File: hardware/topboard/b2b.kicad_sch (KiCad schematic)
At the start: 14 parts

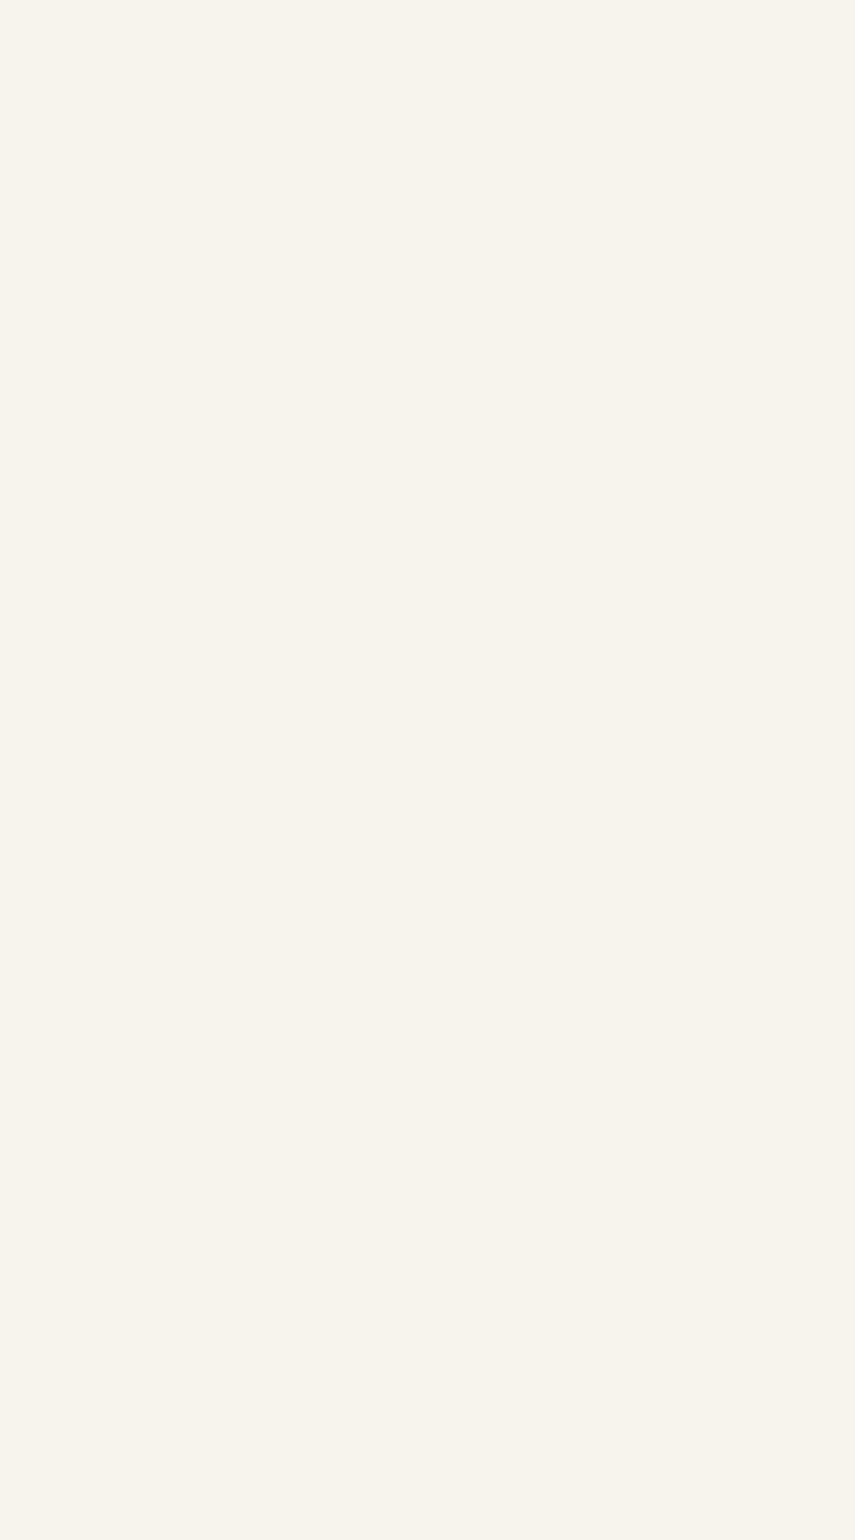
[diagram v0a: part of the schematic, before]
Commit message: Initial pin plan for front b2b connector
Signed-off-by: gatecat <gatecat@ds0.me>
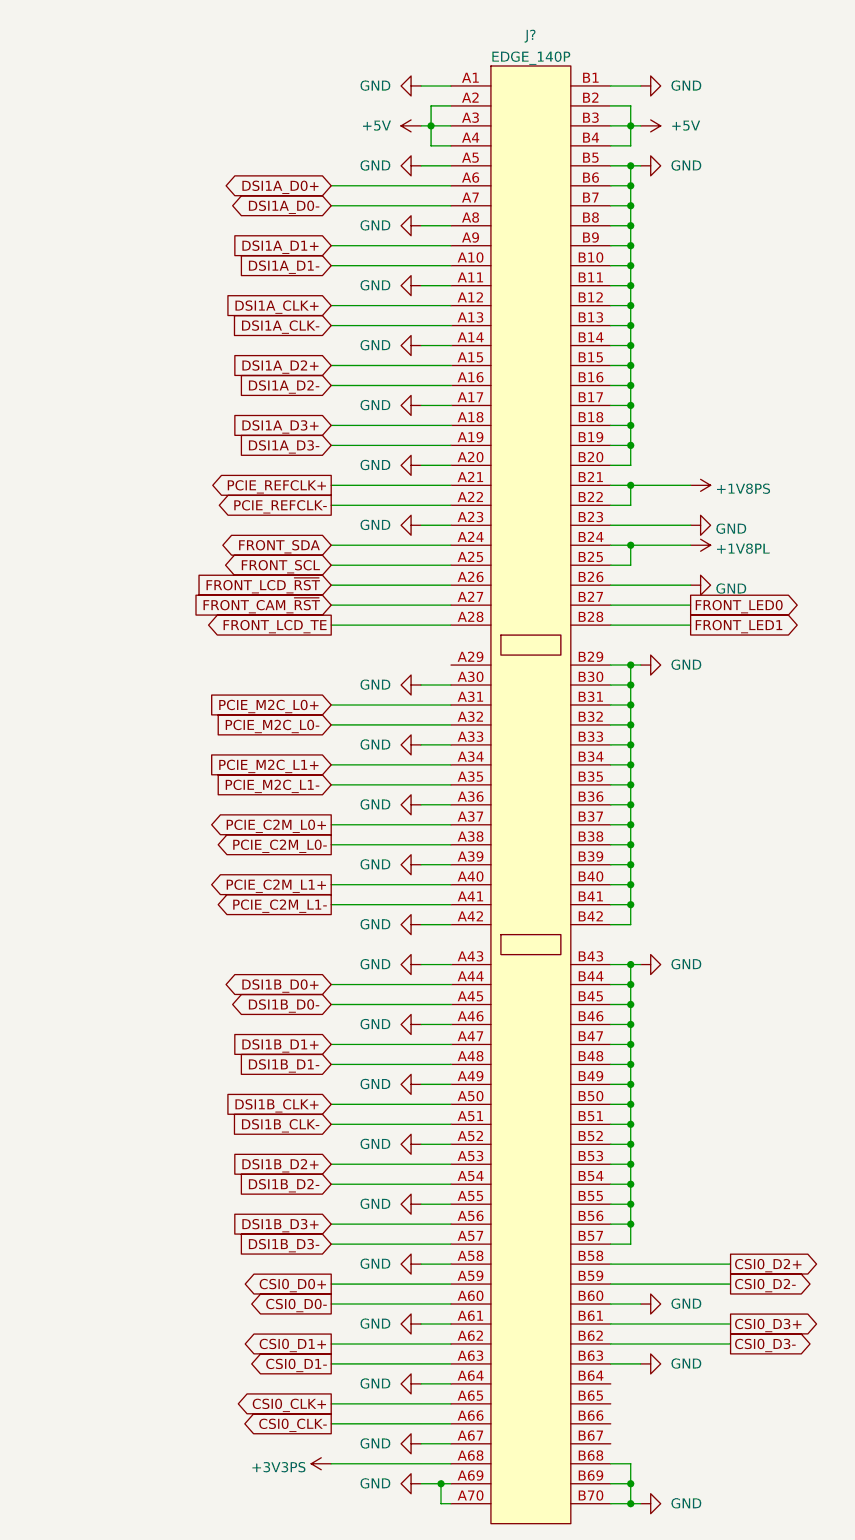
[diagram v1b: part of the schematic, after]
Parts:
- added J?: EDGE_140P, symbol meowality:EDGE_140P
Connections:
- net +1V8PS: now also J?.B21, J?.B22
- net +5V: now also J?.A2, J?.A3, J?.A4, J?.B2, J?.B3, J?.B4
- net GND: now also J?.A1, J?.A11, J?.A14, J?.A17, J?.A20, J?.A23, J?.A30, J?.A33, J?.A36, J?.A39, J?.A42, J?.A43, J?.A46, J?.A49, J?.A5, J?.A52, J?.A55, J?.A58, J?.A61, J?.A64, J?.A67, J?.A69, J?.A70, J?.A8, J?.B1, J?.B10, J?.B11, J?.B12, J?.B13, J?.B14, J?.B15, J?.B16, J?.B17, J?.B18, J?.B19, J?.B20, J?.B23, J?.B26, J?.B29, J?.B30, J?.B31, J?.B32, J?.B33, J?.B34, J?.B35, J?.B36, J?.B37, J?.B38, J?.B39, J?.B40, J?.B41, J?.B42, J?.B43, J?.B44, J?.B45, J?.B46, J?.B47, J?.B48, J?.B49, J?.B5, J?.B50, J?.B51, J?.B52, J?.B53, J?.B54, J?.B55, J?.B56, J?.B57, J?.B6, J?.B60, J?.B63, J?.B68, J?.B69, J?.B7, J?.B70, J?.B8, J?.B9
- new net +1V8PL: J?.B24, J?.B25
- new net +3V3PS: J?.A68
- new net CSI0_CLK+: J?.A65
- new net CSI0_CLK-: J?.A66
- new net CSI0_D0+: J?.A59
- new net CSI0_D0-: J?.A60
- new net CSI0_D1+: J?.A62
- new net CSI0_D1-: J?.A63
- new net CSI0_D2+: J?.B58
- new net CSI0_D2-: J?.B59
- new net CSI0_D3+: J?.B61
- new net CSI0_D3-: J?.B62
- new net DSI1A_CLK+: J?.A12
- new net DSI1A_CLK-: J?.A13
- new net DSI1A_D0+: J?.A6
- new net DSI1A_D0-: J?.A7
- new net DSI1A_D1+: J?.A9
- new net DSI1A_D1-: J?.A10
- new net DSI1A_D2+: J?.A15
- new net DSI1A_D2-: J?.A16
- new net DSI1A_D3+: J?.A18
- new net DSI1A_D3-: J?.A19
- new net DSI1B_CLK+: J?.A50
- new net DSI1B_CLK-: J?.A51
- new net DSI1B_D0+: J?.A44
- new net DSI1B_D0-: J?.A45
- new net DSI1B_D1+: J?.A47
- new net DSI1B_D1-: J?.A48
- new net DSI1B_D2+: J?.A53
- new net DSI1B_D2-: J?.A54
- new net DSI1B_D3+: J?.A56
- new net DSI1B_D3-: J?.A57
- new net FRONT_CAM_~{RST}: J?.A27
- new net FRONT_LCD_TE: J?.A28
- new net FRONT_LCD_~{RST}: J?.A26
- new net FRONT_LED0: J?.B27
- new net FRONT_LED1: J?.B28
- new net FRONT_SCL: J?.A25
- new net FRONT_SDA: J?.A24
- new net PCIE_C2M_L0+: J?.A37
- new net PCIE_C2M_L0-: J?.A38
- new net PCIE_C2M_L1+: J?.A40
- new net PCIE_C2M_L1-: J?.A41
- new net PCIE_M2C_L0+: J?.A31
- new net PCIE_M2C_L0-: J?.A32
- new net PCIE_M2C_L1+: J?.A34
- new net PCIE_M2C_L1-: J?.A35
- new net PCIE_REFCLK+: J?.A21
- new net PCIE_REFCLK-: J?.A22

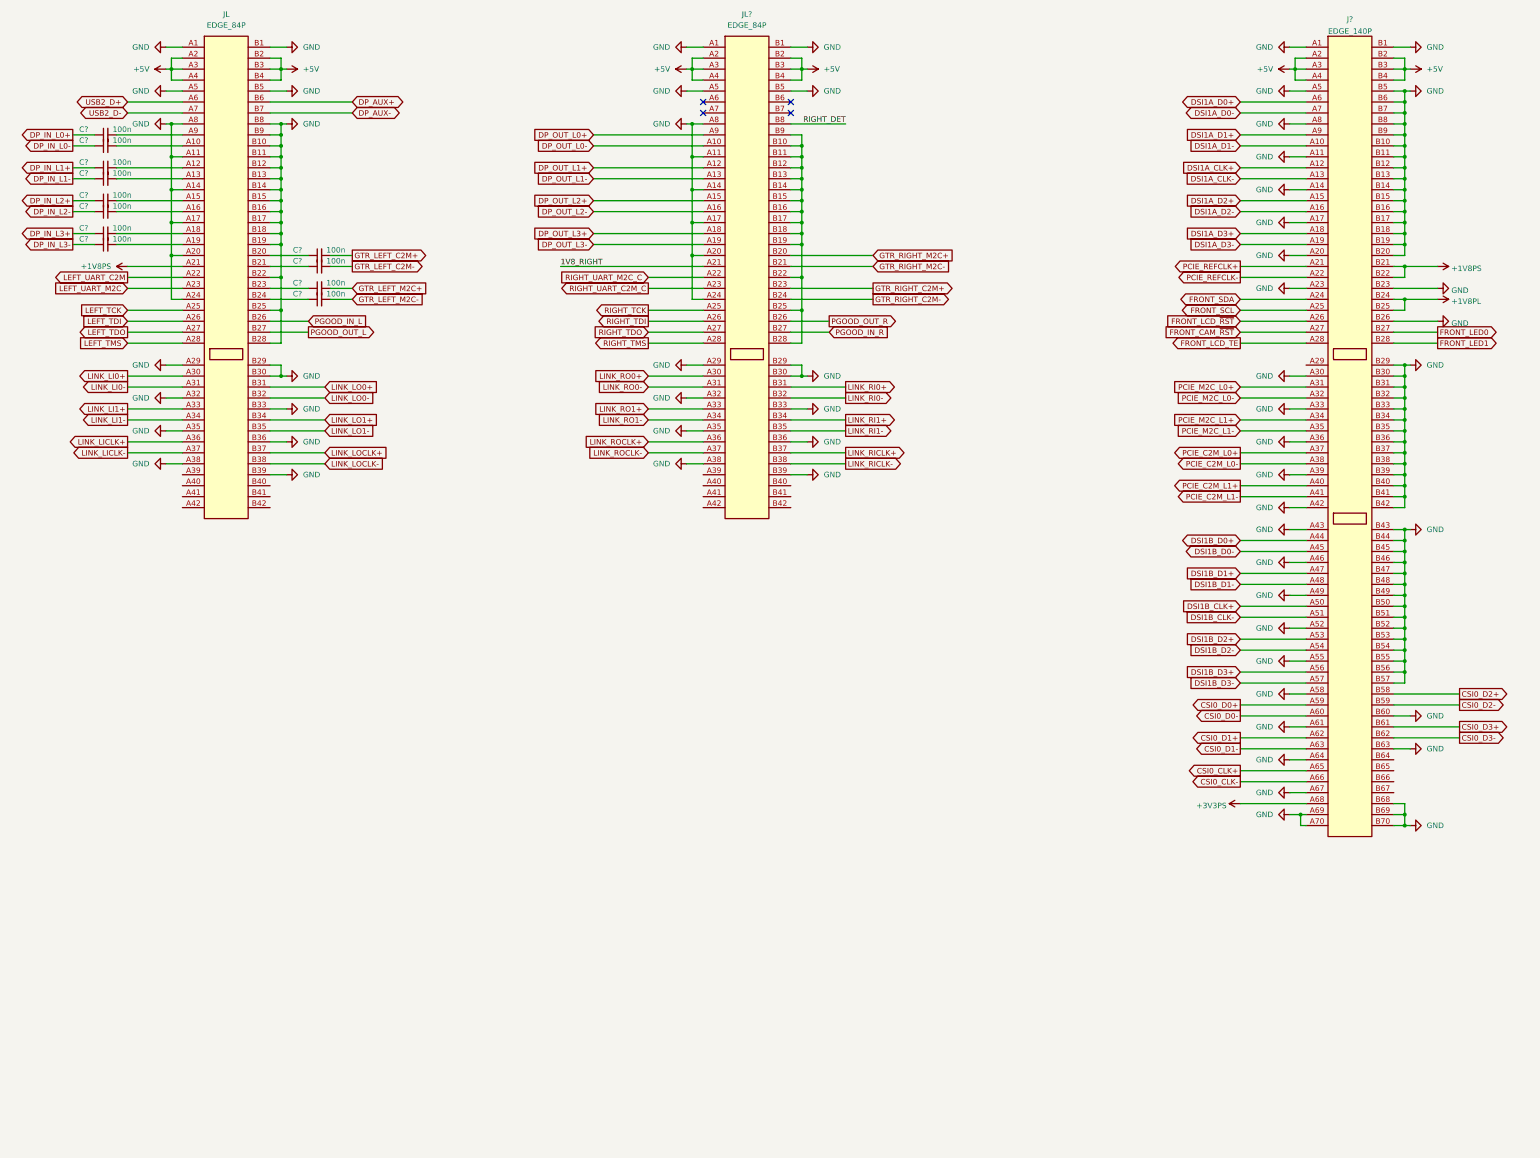
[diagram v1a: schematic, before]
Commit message: SD card, ULPI PHY, JTAG/UART
Signed-off-by: gatecat <gatecat@ds0.me>
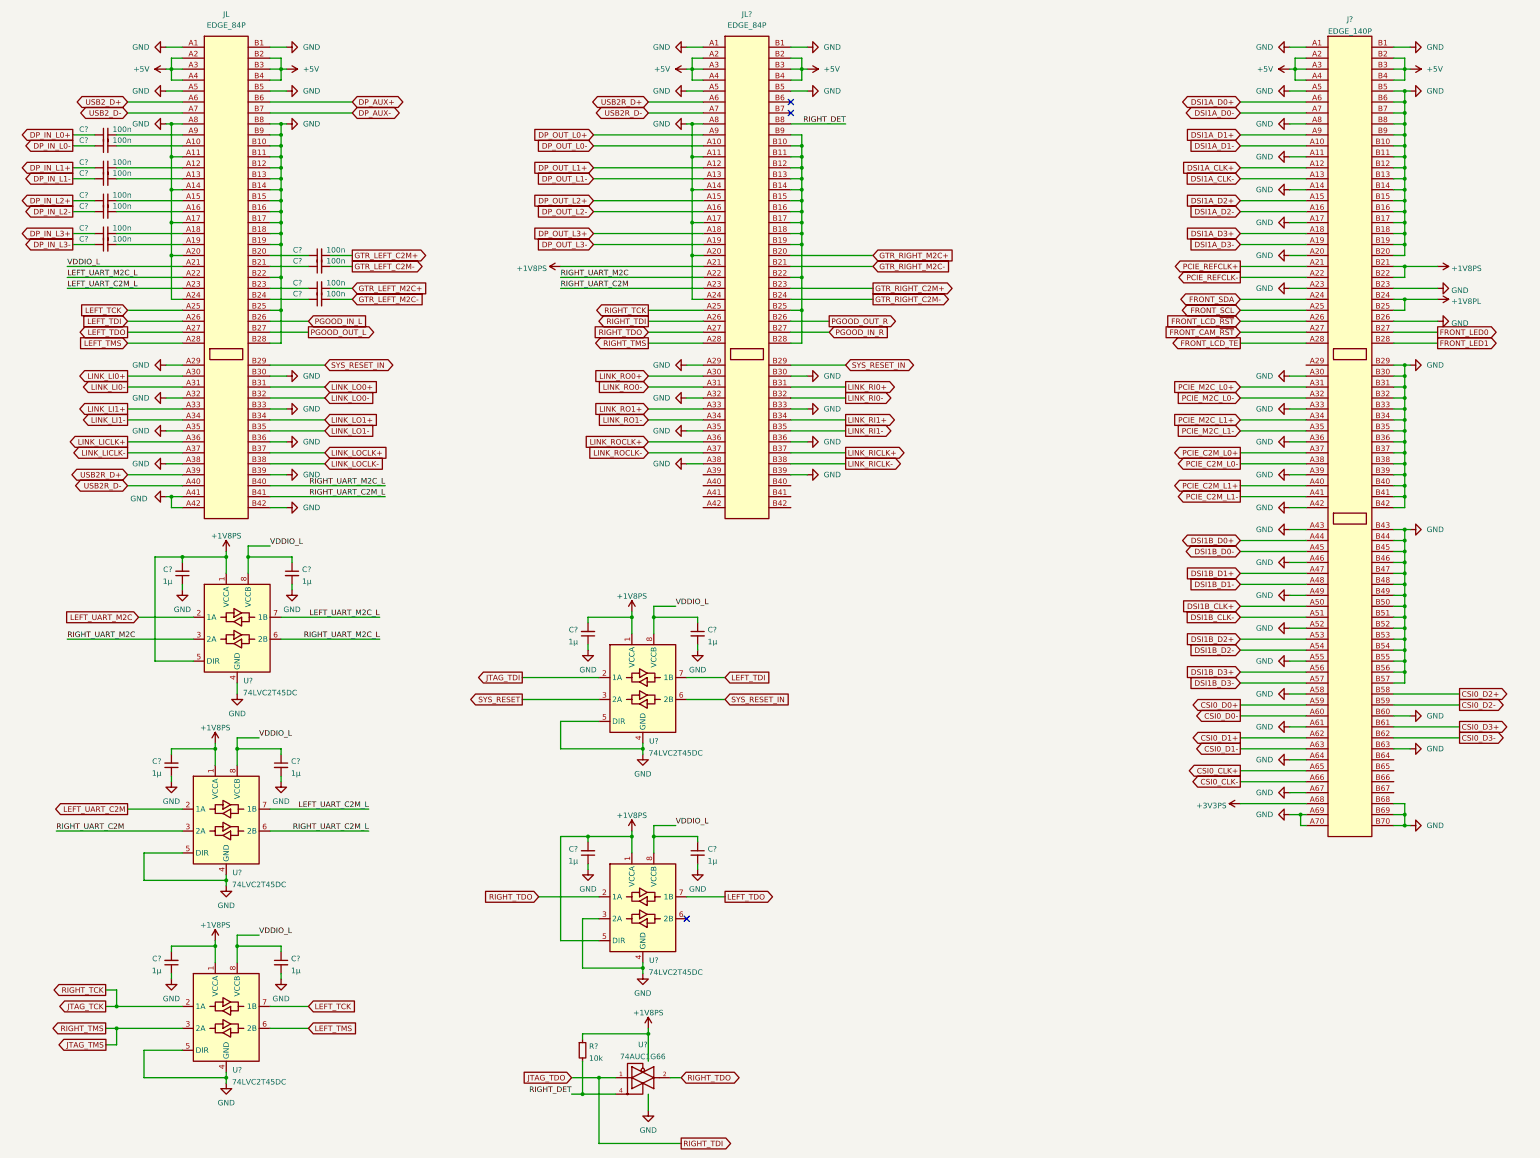
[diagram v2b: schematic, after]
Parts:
- added C? (x10): 1µ, symbol Device:C_Small
- added R?: 10k, symbol Device:R_Small
- added U? (x5): 74LVC2T45DC, Package_SO:VSSOP-8_2.3x2mm_P0.5mm, symbol Logic_LevelTranslator:74LVC2T45DC
- added U?: 74AUC1G66, symbol 74xGxx:74AUC1G66
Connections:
- net 1V8_RIGHT is gone; now on net +1V8PS: JL?.A21
- net +1V8PS: now also C?.2, C?.2, C?.2, C?.2, C?.2, R?.1, U?.1 (VCCA), U?.1 (VCCA), U?.1 (VCCA), U?.1 (VCCA), U?.1 (VCCA), U?.5 (DIR), U?.5 (DIR), U?.5 (VCC); no longer JL.A21
- net GND: now also JL.A41, JL.A42, JL.B42, C?.1, C?.1, C?.1, C?.1, C?.1, C?.2, C?.2, C?.2, C?.2, C?.2, U?.3 (2A), U?.3 (GND), U?.4 (GND), U?.4 (GND), U?.4 (GND), U?.4 (GND), U?.4 (GND), U?.5 (DIR), U?.5 (DIR), U?.5 (DIR); no longer JL.B29, JL?.B29
- net LEFT_TCK: now also U?.7 (1B)
- net LEFT_TDI: now also U?.7 (1B)
- net LEFT_TDO: now also U?.7 (1B)
- net LEFT_TMS: now also U?.6 (2B)
- net LEFT_UART_C2M: now also U?.2 (1A); no longer JL.A22
- net LEFT_UART_M2C: now also U?.2 (1A); no longer JL.A23
- net RIGHT_DET: now also R?.2, U?.4
- net RIGHT_TDO: now also U?.2, U?.2 (1A)
- net USB2R_D+: now reaches JL?.A6
- net USB2R_D+: now also JL.A39
- net USB2R_D-: now reaches JL?.A7
- net USB2R_D-: now also JL.A40
- net RIGHT_UART_M2C_L: now reaches JL.B40
- net RIGHT_UART_M2C_L: now also U?.6 (2B)
- net RIGHT_UART_C2M_L: now reaches JL.B41
- net RIGHT_UART_C2M_L: now also U?.6 (2B)
- net RIGHT_TCK renamed JTAG_TCK
- net JTAG_TCK: now also U?.2 (1A)
- net RIGHT_TDI renamed JTAG_TDO
- net JTAG_TDO: now also U?.1
- net RIGHT_TMS renamed JTAG_TMS
- net JTAG_TMS: now also U?.3 (2A)
- net RIGHT_UART_C2M_C renamed RIGHT_UART_C2M
- net RIGHT_UART_C2M: now also U?.3 (2A)
- net RIGHT_UART_M2C_C renamed RIGHT_UART_M2C
- net RIGHT_UART_M2C: now also U?.3 (2A)
- new net JTAG_TDI: U?.2 (1A)
- new net LEFT_UART_C2M_L: JL.A23, U?.7 (1B)
- new net LEFT_UART_M2C_L: JL.A22, U?.7 (1B)
- new net SYS_RESET: U?.3 (2A)
- new net SYS_RESET_IN: JL.B29, JL?.B29, U?.6 (2B)
- new net VDDIO_L: C?.1, C?.1, C?.1, C?.1, C?.1, JL.A21, U?.8 (VCCB), U?.8 (VCCB), U?.8 (VCCB), U?.8 (VCCB), U?.8 (VCCB)
- no-connect marks 4 -> 3
